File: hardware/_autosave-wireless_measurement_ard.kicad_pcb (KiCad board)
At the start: 4 copper layers, 30.3 x 17.8 mm, 25 parts, among them J1 Conn_01x08, SW1 SW_SPDT, U1 EFM8LB1, U2 JDY-08, U3 MCP16415, U4 MAX44284, U5 DRV5021

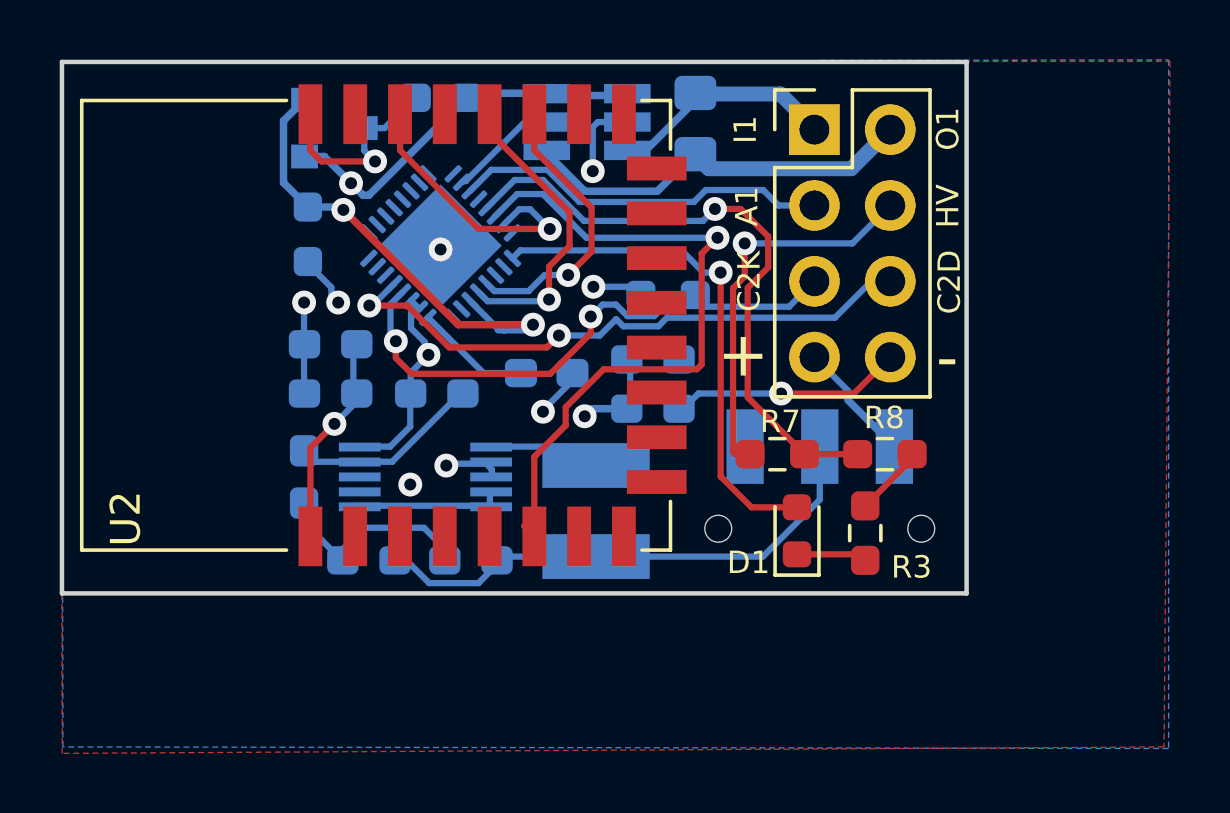
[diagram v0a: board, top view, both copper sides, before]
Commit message: label changes
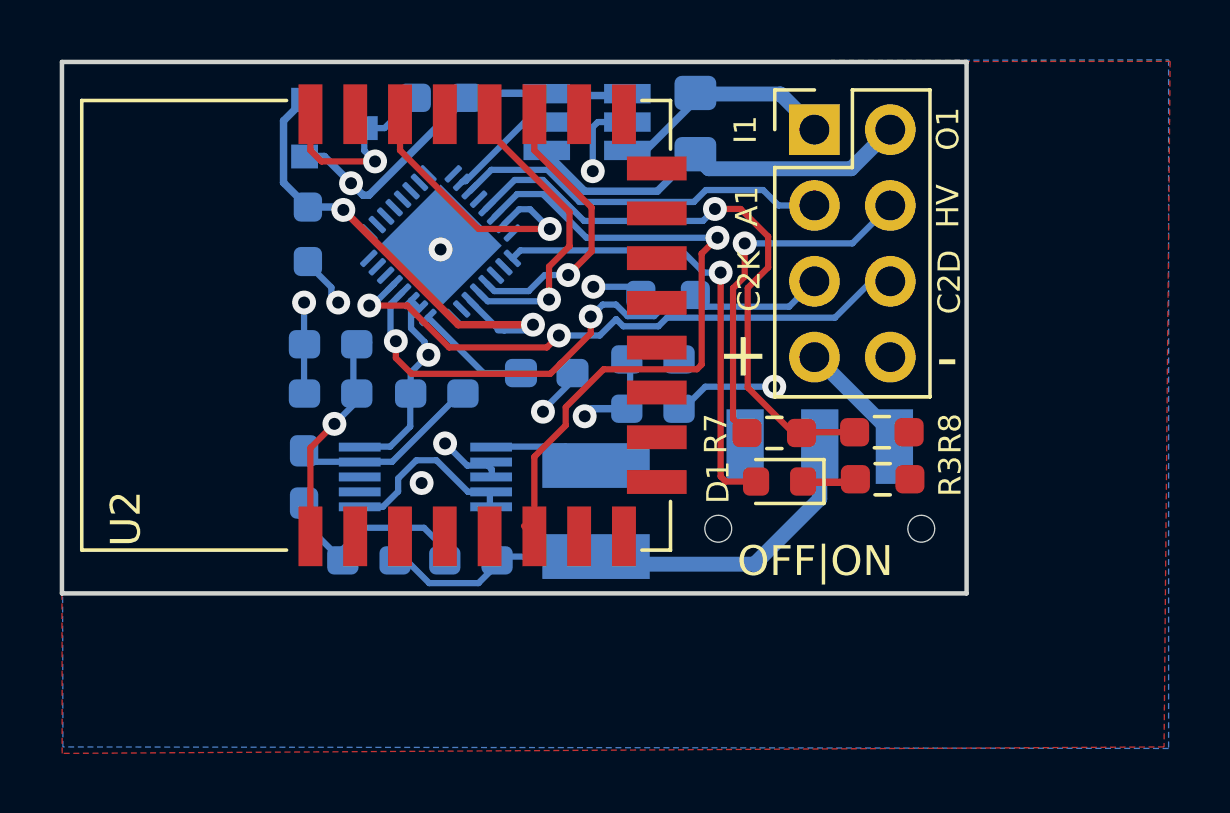
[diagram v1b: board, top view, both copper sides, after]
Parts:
- moved R3 1.90 mm to (137.5, 89.0), turned to 0 degrees
- moved D1 1.75 mm to (134.0, 89.1), turned to 180 degrees
- moved R8 0.74 mm to (137.5, 87.4)
- moved R7 0.72 mm to (133.9, 87.4)
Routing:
- net GND: track 32.7 -> 26.4 mm
- net LED: track 17.2 -> 15.5 mm
- net VIN: track 24.9 -> 26.5 mm
- net VHIGH: track 13.1 -> 12.1 mm
- net Net-(D1-Pad1): track 2.37 -> 1.50 mm
- net A3: track 21.1 -> 20.5 mm
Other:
- board text added: "OFF|ON"
